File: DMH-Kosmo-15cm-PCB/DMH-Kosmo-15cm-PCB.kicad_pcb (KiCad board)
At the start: 2 copper layers, 49 x 175 mm, 0 parts

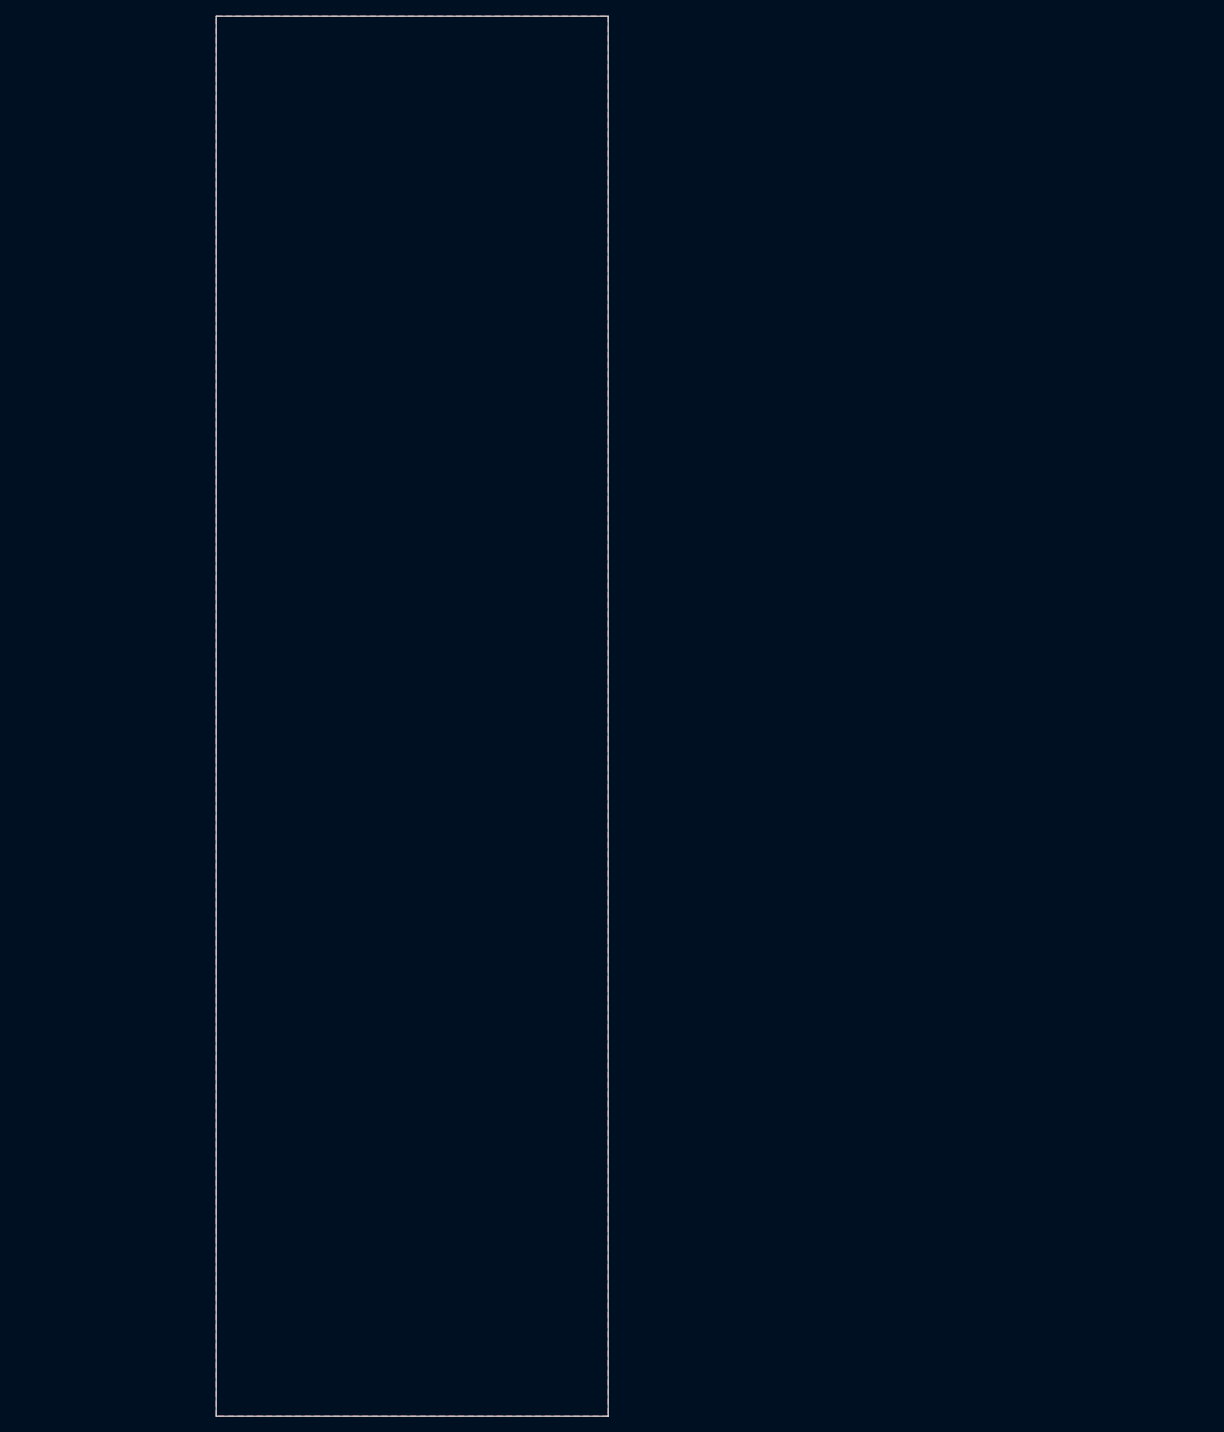
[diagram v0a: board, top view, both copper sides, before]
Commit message: Added 15cm templates
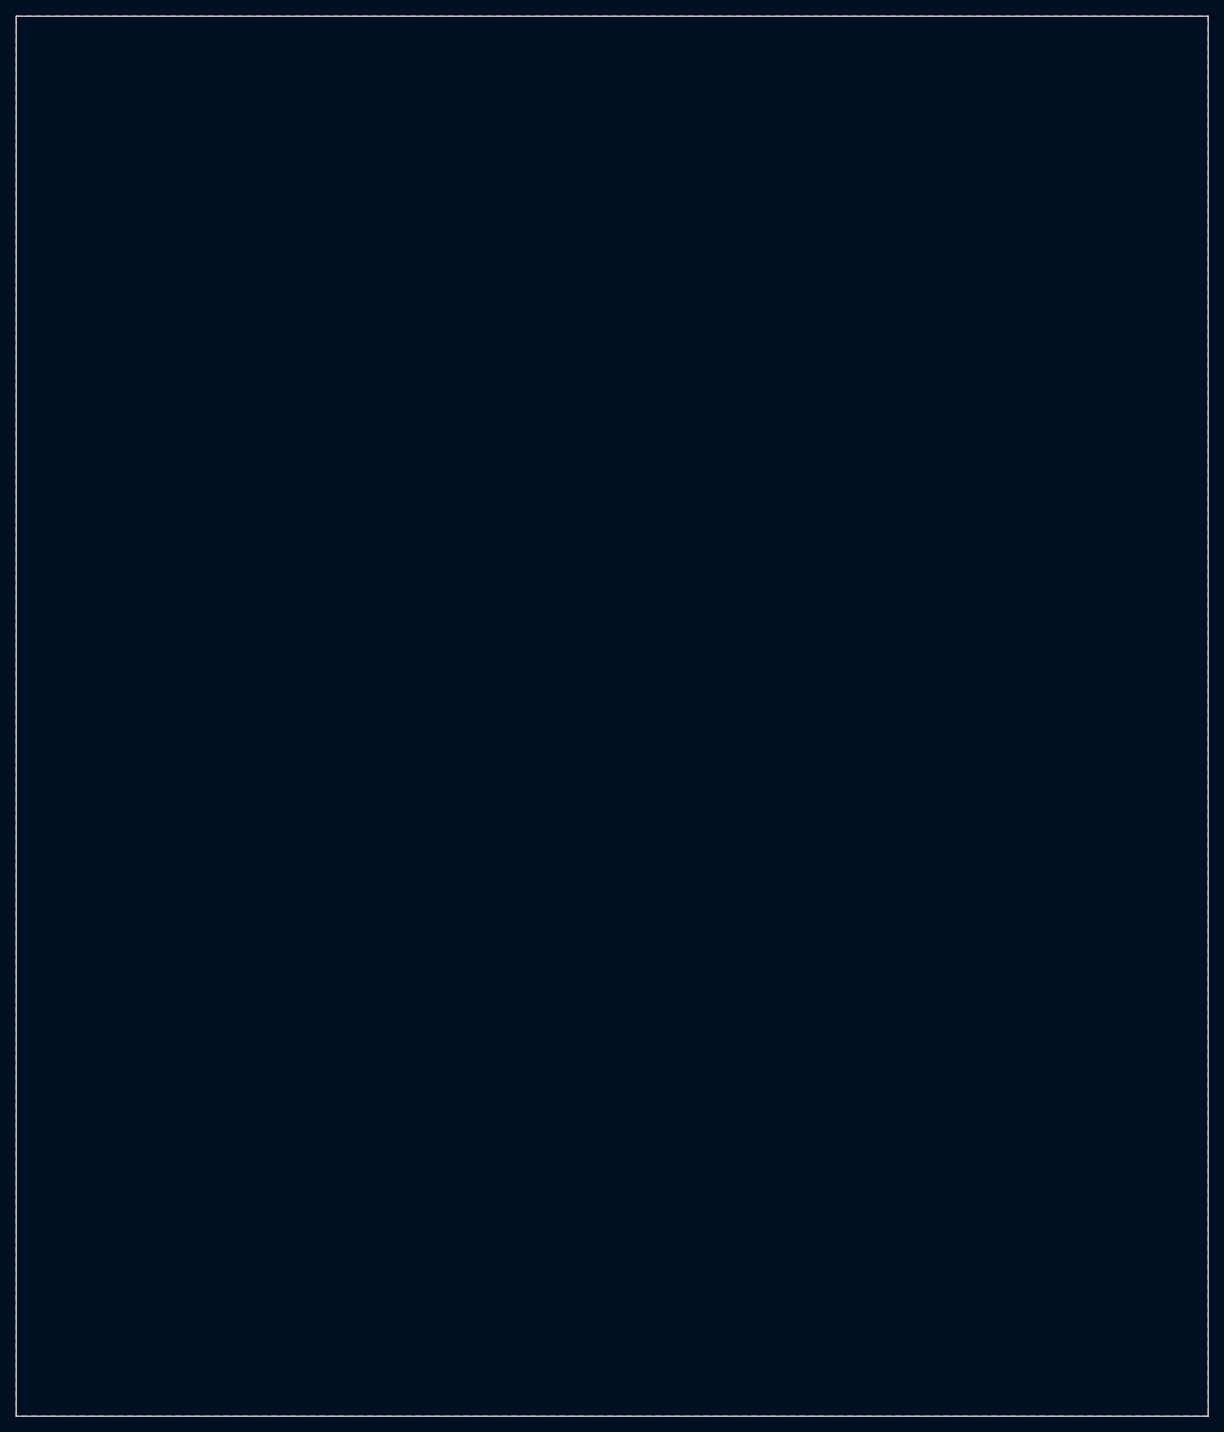
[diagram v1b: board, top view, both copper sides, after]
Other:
- board size 49 x 175 mm -> 149 x 175 mm
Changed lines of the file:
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@@
 		(capping no)
 		(filling no)
-		(grid_origin 50 30)
+		(grid_origin 25 30)
 		(pcbplotparams
 			(layerselection 0x00000000_00000000_55555555_5755f5ff)
@@
 	)
 	(gr_rect
-		(start 70 212.75)
-		(end 80 214.75)
+		(start 95 212.75)
+		(end 105 214.75)
 		(stroke
 			(width 0.1)
@@
 	)
 	(gr_circle
-		(center 58.5 153.25)
-		(end 63.25 153.25)
-		(stroke
-			(width 0.1)
-			(type default)
-		)
-		(fill no)
-		(layer "Cmts.User")
-	)
-	(gr_circle
-		(center 58.5 171.75)
-		(end 63.25 171.75)
-		(stroke
-			(width 0.1)
-			(type default)
-		)
-		(fill no)
-		(layer "Cmts.User")
-	)
-	(gr_circle
-		(center 58.5 190.25)
-		(end 63.25 190.25)
-		(stroke
-			(width 0.1)
-			(type default)
-		)
-		(fill no)
-		(layer "Cmts.User")
-	)
-	(gr_circle
-		(center 58.5 208.75)
-		(end 63.25 208.75)
-		(stroke
-			(width 0.1)
-			(type default)
-		)
-		(fill no)
-		(layer "Cmts.User")
-	)
-	(gr_circle
-		(center 75 153.25)
-		(end 79.75 153.25)
-		(stroke
-			(width 0.1)
-			(type default)
-		)
-		(fill no)
-		(layer "Cmts.User")
-	)
-	(gr_circle
-		(center 75 171.75)
-		(end 79.75 171.75)
-		(stroke
-			(width 0.1)
-			(type default)
-		)
-		(fill no)
-		(layer "Cmts.User")
-	)
-	(gr_circle
-		(center 75 190.25)
-		(end 79.75 190.25)
-		(stroke
-			(width 0.1)
-			(type default)
-		)
-		(fill no)
-		(layer "Cmts.User")
-	)
-	(gr_circle
-		(center 75 208.75)
-		(end 79.75 208.75)
-		(stroke
-			(width 0.1)
-			(type default)
-		)
-		(fill no)
-		(layer "Cmts.User")
-	)
-	(gr_circle
-		(center 91.5 153.25)
-		(end 96.25 153.25)
-		(stroke
-			(width 0.1)
-			(type default)
-		)
-		(fill no)
-		(layer "Cmts.User")
-	)
-	(gr_circle
-		(center 91.5 171.75)
-		(end 96.25 171.75)
-		(stroke
-			(width 0.1)
-			(type default)
-		)
-		(fill no)
-		(layer "Cmts.User")
-	)
-	(gr_circle
-		(center 91.5 190.25)
-		(end 96.25 190.25)
-		(stroke
-			(width 0.1)
-			(type default)
-		)
-		(fill no)
-		(layer "Cmts.User")
-	)
-	(gr_circle
-		(center 91.5 208.75)
-		(end 96.25 208.75)
+		(center 33.5 171.75)
+		(end 38.25 171.75)
+		(stroke
+			(width 0.1)
+			(type default)
+		)
+		(fill no)
+		(layer "Cmts.User")
+	)
+	(gr_circle
+		(center 33.5 190.25)
+		(end 38.25 190.25)
+		(stroke
+			(width 0.1)
+			(type default)
+		)
+		(fill no)
+		(layer "Cmts.User")
+	)
+	(gr_circle
+		(center 33.5 208.75)
+		(end 38.25 208.75)
+		(stroke
+			(width 0.1)
+			(type default)
+		)
+		(fill no)
+		(layer "Cmts.User")
+	)
+	(gr_circle
+		(center 50 190.25)
+		(end 54.75 190.25)
+		(stroke
+			(width 0.1)
+			(type default)
+		)
+		(fill no)
+		(layer "Cmts.User")
+	)
+	(gr_circle
+		(center 50 208.75)
+		(end 54.75 208.75)
+		(stroke
+			(width 0.1)
+			(type default)
+		)
+		(fill no)
+		(layer "Cmts.User")
+	)
+	(gr_circle
+		(center 66.5 190.25)
+		(end 71.25 190.25)
+		(stroke
+			(width 0.1)
+			(type default)
+		)
+		(fill no)
+		(layer "Cmts.User")
+	)
+	(gr_circle
+		(center 66.5 208.75)
+		(end 71.25 208.75)
+		(stroke
+			(width 0.1)
+			(type default)
+		)
+		(fill no)
+		(layer "Cmts.User")
+	)
+	(gr_circle
+		(center 83 190.25)
+		(end 87.75 190.25)
+		(stroke
+			(width 0.1)
+			(type default)
+		)
+		(fill no)
+		(layer "Cmts.User")
+	)
+	(gr_circle
+		(center 83 208.75)
+		(end 87.75 208.75)
+		(stroke
+			(width 0.1)
+			(type default)
+		)
+		(fill no)
+		(layer "Cmts.User")
+	)
+	(gr_circle
+		(center 100 190.25)
+		(end 104.75 190.25)
+		(stroke
+			(width 0.1)
+			(type default)
+		)
+		(fill no)
+		(layer "Cmts.User")
+	)
+	(gr_circle
+		(center 100 208.75)
+		(end 104.75 208.75)
+		(stroke
+			(width 0.1)
+			(type default)
+		)
+		(fill no)
+		(layer "Cmts.User")
+	)
+	(gr_circle
+		(center 117 190.25)
+		(end 121.75 190.25)
+		(stroke
+			(width 0.1)
+			(type default)
+		)
+		(fill no)
+		(layer "Cmts.User")
+	)
+	(gr_circle
+		(center 117 208.75)
+		(end 121.75 208.75)
+		(stroke
+			(width 0.1)
+			(type default)
+		)
+		(fill no)
+		(layer "Cmts.User")
+	)
+	(gr_circle
+		(center 133.5 190.25)
+		(end 138.25 190.25)
+		(stroke
+			(width 0.1)
+			(type default)
+		)
+		(fill no)
+		(layer "Cmts.User")
+	)
+	(gr_circle
+		(center 133.5 208.75)
+		(end 138.25 208.75)
+		(stroke
+			(width 0.1)
+			(type default)
+		)
+		(fill no)
+		(layer "Cmts.User")
+	)
+	(gr_circle
+		(center 150 190.25)
+		(end 154.75 190.25)
+		(stroke
+			(width 0.1)
+			(type default)
+		)
+		(fill no)
+		(layer "Cmts.User")
+	)
+	(gr_circle
+		(center 150 208.75)
+		(end 154.75 208.75)
+		(stroke
+			(width 0.1)
+			(type default)
+		)
+		(fill no)
+		(layer "Cmts.User")
+	)
+	(gr_circle
+		(center 166.5 171.75)
+		(end 171.25 171.75)
+		(stroke
+			(width 0.1)
+			(type default)
+		)
+		(fill no)
+		(layer "Cmts.User")
+	)
+	(gr_circle
+		(center 166.5 190.25)
+		(end 171.25 190.25)
+		(stroke
+			(width 0.1)
+			(type default)
+		)
+		(fill no)
+		(layer "Cmts.User")
+	)
+	(gr_circle
+		(center 166.5 208.75)
+		(end 171.25 208.75)
 		(stroke
 			(width 0.1)
@@
 	)
 	(gr_rect
-		(start 50.5 42.5)
-		(end 99.5 217.5)
+		(start 25.5 42.5)
+		(end 174.5 217.5)
 		(stroke
 			(width 0.05)
@@
 	)
 	(gr_rect
-		(start 50 30)
-		(end 100 230)
+		(start 25 30)
+		(end 175 230)
 		(stroke
 			(width 0.1)
@@
 	)
 	(gr_text "Mk1.0 - Month Year"
-		(at 74.75 216.25 0)
+		(at 100 216.25 0)
 		(layer "B.SilkS")
 		(effects
@@
 		(polygon
 			(pts
-				(xy 50.5 42.5) (xy 99.5 42.5) (xy 99.5 217.5) (xy 50.5 217.5)
+				(xy 25.5 42.5) (xy 174.5 42.5) (xy 174.5 217.5) (xy 25.5 217.5)
 			)
 		)
